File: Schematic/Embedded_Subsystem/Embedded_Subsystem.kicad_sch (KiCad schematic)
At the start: 13 parts, among them J1 Micro_SD_Card, J10 Conn_01x06, J11 Conn_01x04, J12 Conn_01x20, J13 Conn_01x08, J2 Conn_01x04, J3 Conn_01x07, J4 Conn_01x04, J5 Conn_01x09, J6 Conn_01x08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

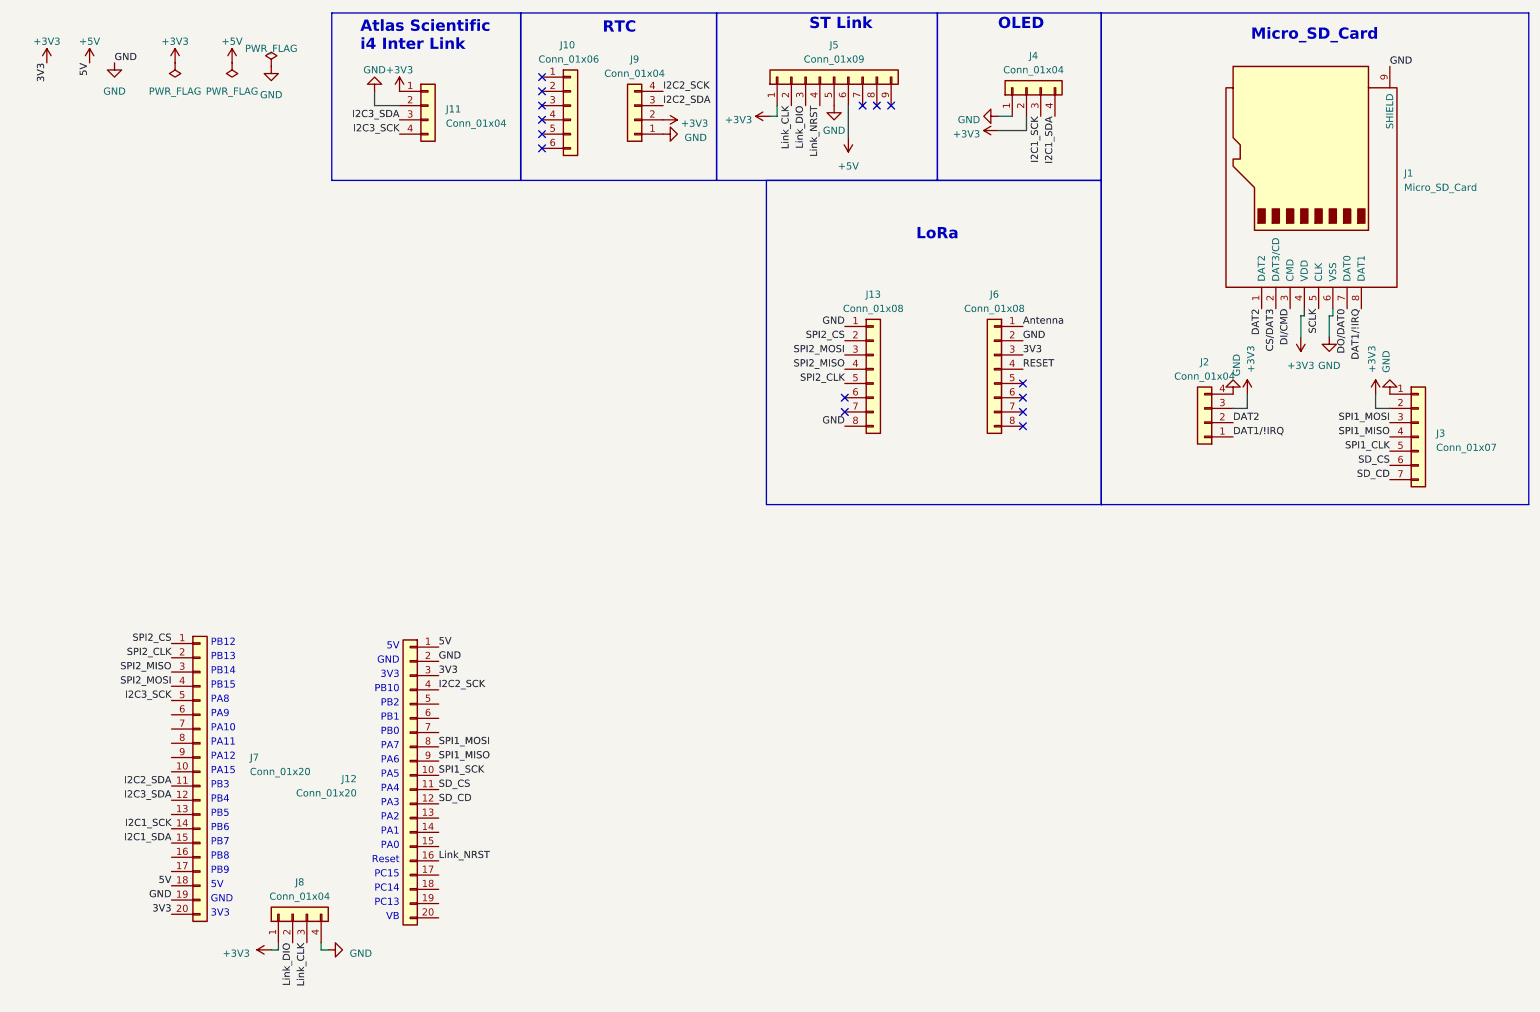
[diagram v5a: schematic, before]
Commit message: Added Robust Code
Added code to re-initilise RTC and OLED when disconnected and reconnected
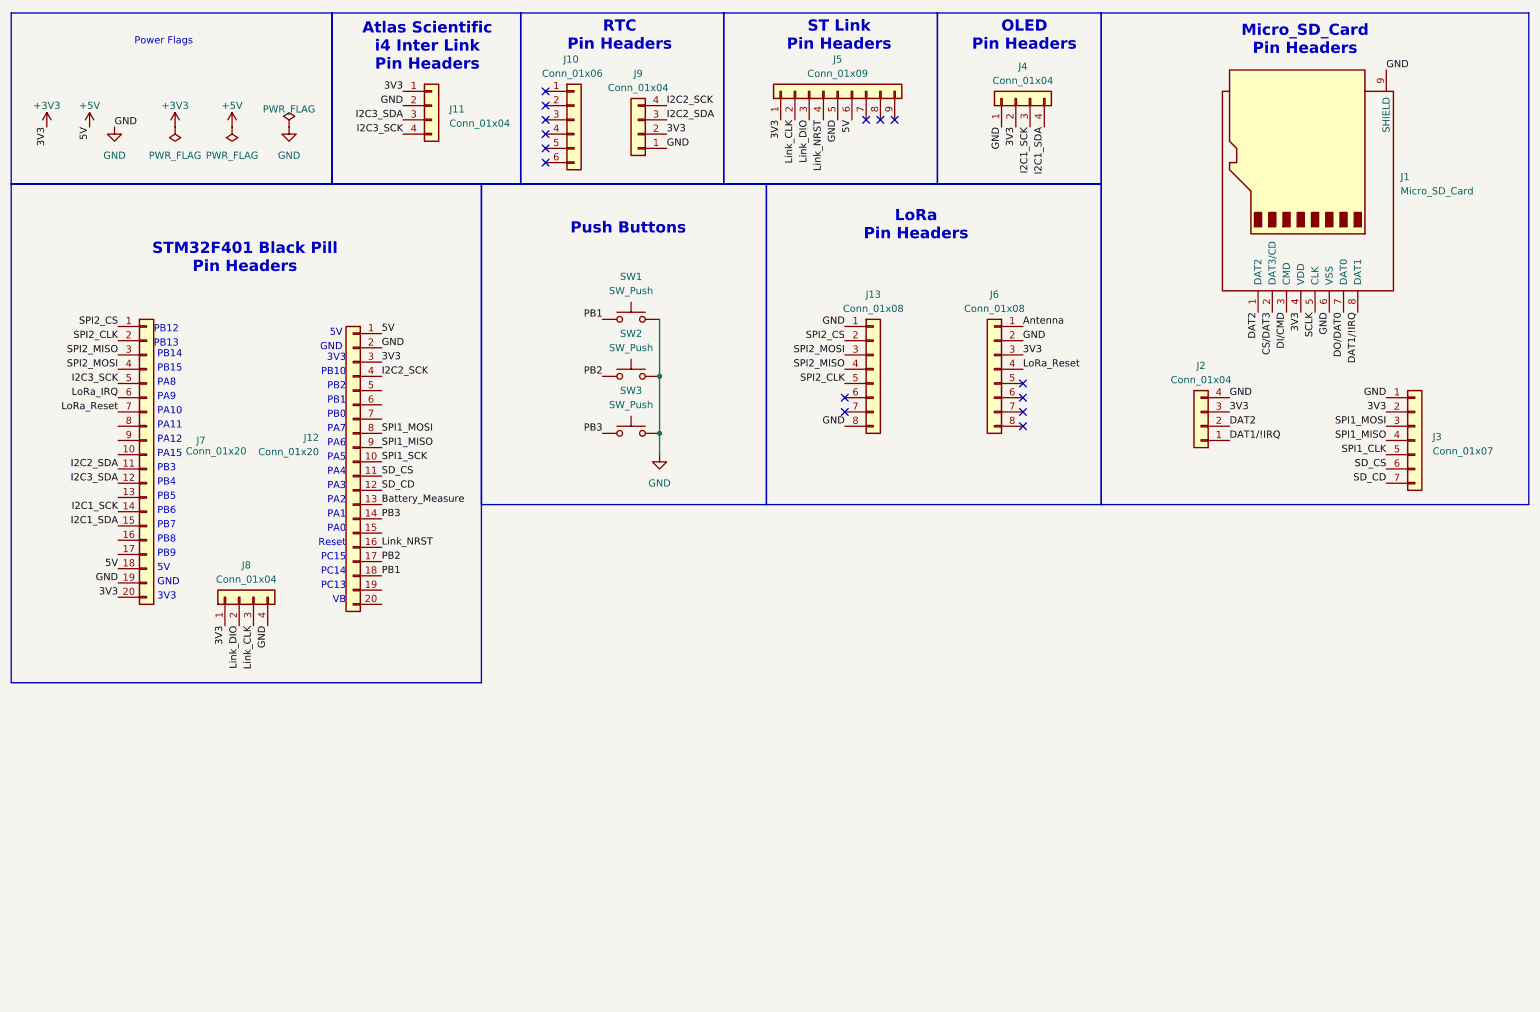
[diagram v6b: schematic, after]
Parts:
- added SW1, SW2, SW3: SW_Push, symbol Switch:SW_Push
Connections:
- net RESET is gone; now on net LoRa_Reset: J6.4 (Pin_4)
- net GND: now also SW1.2, SW2.2, SW3.2
- net Battery_Measure: now reaches J12.13 (Pin_13)
- net PB3: now reaches J12.14 (Pin_14)
- net PB3: now also SW3.1
- net PB2: now reaches J12.17 (Pin_17)
- net PB2: now also SW2.1
- net PB1: now reaches J12.18 (Pin_18)
- net PB1: now also SW1.1
- net LoRa_IRQ: now reaches J7.6 (Pin_6)
- net LoRa_Reset: now reaches J7.7 (Pin_7)
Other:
- note added: "Atlas Scientific i4 Inter Link Pin Headers"
- note added: "LoRa Pin Headers"
- note added: "Micro_SD_Card Pin Headers"
- note added: "OLED Pin Headers"
- note added: "Power Flags"
- note added: "Push Buttons"
- note added: "RTC Pin Headers"
- note added: "ST Link Pin Headers"
- note added: "STM32F401 Black Pill Pin Headers"
- note removed: "Atlas Scientific i4 Inter Link"
- note removed: "LoRa"
- note removed: "Micro_SD_Card"
- note removed: "OLED"
- note removed: "RTC"
- note removed: "ST Link"
- moved on the sheet: J1, J10, J11, J12, J2, J3, J4, J5, J7, J8, J9
